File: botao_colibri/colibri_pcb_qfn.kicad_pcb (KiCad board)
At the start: 2 copper layers, 72.5 x 47.1 mm, 32 parts, among them J2 TC2030, J3 Conn_01x02, J4 PJ-307C

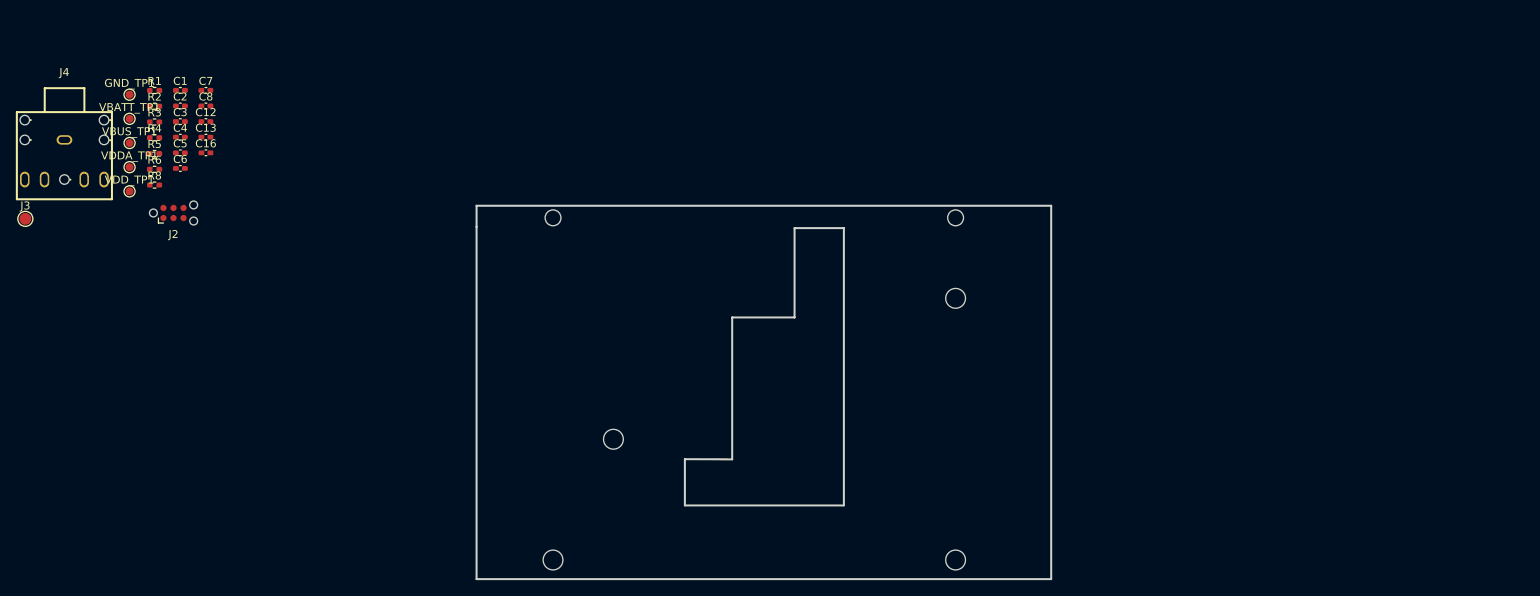
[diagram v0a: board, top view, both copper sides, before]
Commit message: Posicionamento inicial dos componentes na pcb e alguns ajustes no esquemático
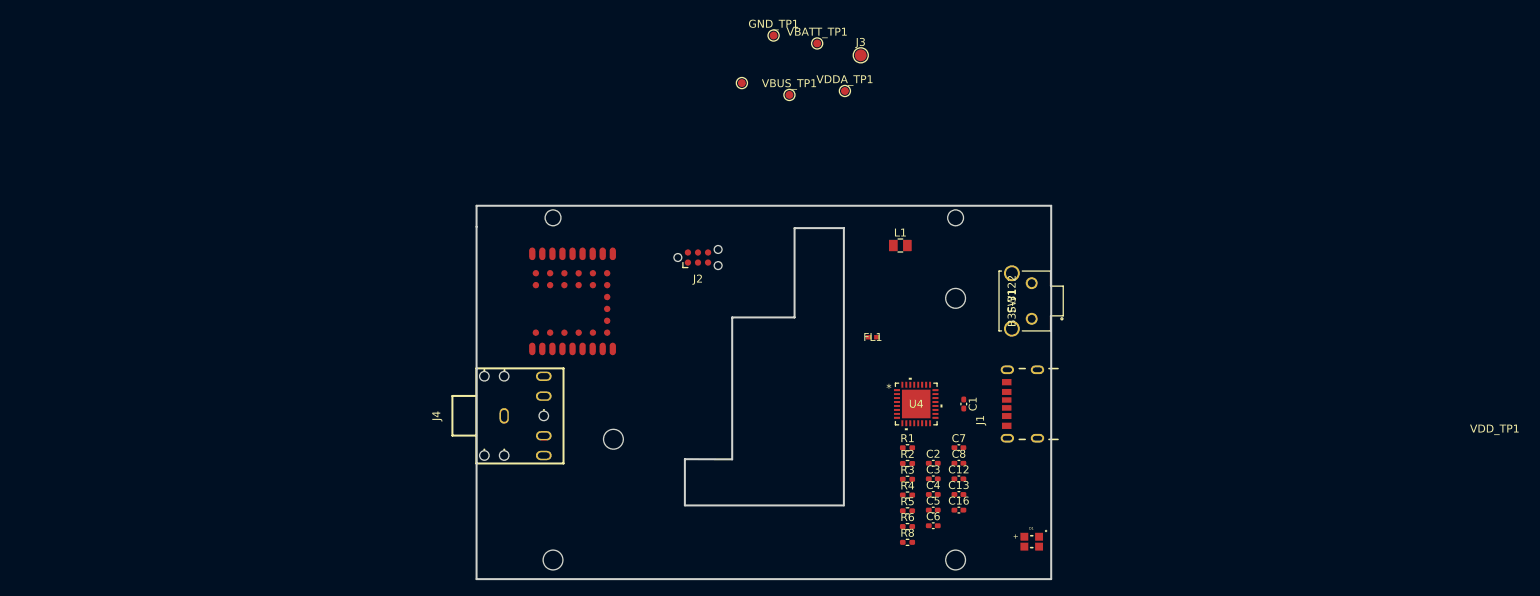
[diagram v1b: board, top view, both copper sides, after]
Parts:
- added D1: WL-SFCD_0805, colibri-v4:WL-SFCD_0805, F.Cu at (194.1, 114.9)
- added FL1: BLM15AG121SN1D, colibri-v4:IND_BLM15_0402_MUR, F.Cu at (174.0, 89.1)
- added J1: USB4970-00-A_REVA, colibri-v4:GCT_USB4970-00-A_REVA, F.Cu at (194.0, 97.5)
- added L1: 2.2µH, colibri-v4:LQM21PN2R2MGRD, F.Cu at (177.5, 77.5)
- added SW1: B3F-3122, colibri-v4:B3F-3122, F.Cu at (194.1, 86.8)
- added U1: ME54BS12, colibri-v4:ME54BS12_V1.0, F.Cu at (141.9, 90.5)
- added U4: NPM1300-QEAA-R7, colibri-v4:NPM1300_QFN32_5X5_NOR, F.Cu at (179.5, 97.5)
- moved J3 107.4 mm to (172.5, 53.5)
- moved C1 106.5 mm to (185.5, 97.5), turned to -90 degrees
- moved C12 105.2 mm to (184.9, 107.0)
- moved C13 105.2 mm to (184.9, 108.9)
- moved C16 105.2 mm to (184.9, 110.9)
- moved C2 105.2 mm to (181.7, 105.0)
- moved C3 105.2 mm to (181.7, 107.0)
- moved C4 105.2 mm to (181.7, 108.9)
- moved C5 105.2 mm to (181.7, 110.9)
- moved C6 105.2 mm to (181.7, 112.9)
- moved C7 105.2 mm to (184.9, 103.0)
- moved C8 105.2 mm to (184.9, 105.0)
- moved R1 105.2 mm to (178.4, 103.0)
- moved R2 105.2 mm to (178.4, 105.0)
- moved R3 105.2 mm to (178.4, 107.0)
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
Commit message: Avanço nos posicionamentos
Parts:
- moved R6 41.1 mm to (144.0, 90.5), turned to 180 degrees
- moved R4 40.4 mm to (140.9, 94.0)
- moved R5 38.3 mm to (144.1, 94.0), turned to 180 degrees
- moved C6 34.0 mm to (178.4, 79.0), turned to 180 degrees
- moved C5 29.1 mm to (178.4, 82.0), turned to 180 degrees
- moved C4 23.6 mm to (178.4, 85.5), turned to 180 degrees
- moved C13 21.4 mm to (178.5, 88.5), turned to 180 degrees
- moved D1 21.2 mm to (172.9, 116.9)
- moved C16 20.4 mm to (178.5, 91.5), turned to 180 degrees
- moved L1 19.9 mm to (174.0, 97.1), turned to -90 degrees
- moved C1 15.5 mm to (181.4, 112.5), turned to 0 degrees
- moved C2 15.3 mm to (174.5, 91.5)
- moved FL1 13.9 mm to (174.0, 103.0), turned to -90 degrees
- moved R8 11.9 mm to (181.5, 103.5), turned to 180 degrees
- moved R1 9.70 mm to (186.4, 108.5), turned to 180 degrees
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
